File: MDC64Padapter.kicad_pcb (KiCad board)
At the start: 2 copper layers, 42.7 x 31 mm, 34 parts, among them J1 DB9_F_TO_C64, J2 DB9_M_TO_PAD, Q1 BC847, Q2 BC847, SW1 MODE, U1 74ACT08, U2 74ACT373, U3 74ACT157, U4 74ACT373, U5 74AHC1G04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

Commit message: Update PCB
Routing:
- net GND: track 242.2 -> 244.7 mm
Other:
- board text added: "Rev.0"
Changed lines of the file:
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@@
 		(tags "capacitor handsolder")
 		(property "Reference" "C7"
-			(at 0 0 0)
+			(at -2.54 -0.0885 90)
 			(layer "F.SilkS")
 			(effects
 				(font
-					(size 1 1)
-					(thickness 0.15)
+					(size 0.5 0.8)
+					(thickness 0.1)
 				)
 			)
 		)
 		(property "Value" "100nF"
-			(at 0 1.85 0)
-			(layer "F.Fab")
+			(at 0 0 0)
+			(layer "F.SilkS")
 			(effects
 				(font
-					(size 1 1)
-					(thickness 0.15)
+					(size 0.8 0.4)
+					(thickness 0.08)
 				)
 			)
@@
 		)
 		(property "Value" "10nF"
-			(at 0 1.85 90)
-			(layer "F.Fab")
+			(at 0 0 90)
+			(layer "F.SilkS")
 			(effects
 				(font
-					(size 1 1)
-					(thickness 0.15)
+					(size 0.8 0.5)
+					(thickness 0.1)
+					(bold yes)
 				)
 			)
@@
 		)
 		(property "Value" "10uF"
-			(at 0 1.85 90)
-			(layer "F.Fab")
+			(at 0 0 270)
+			(layer "F.SilkS")
 			(effects
 				(font
-					(size 1 1)
-					(thickness 0.15)
+					(size 0.8 0.5)
+					(thickness 0.08)
 				)
 			)
@@
 		(layer "Edge.Cuts")
 	)
+	(gr_text "Rev.0"
+		(at 65.151 128.397 0)
+		(layer "B.Cu")
+		(effects
+			(font
+				(size 1.5 1.5)
+				(thickness 0.3)
+				(bold yes)
+			)
+			(justify mirror)
+		)
+	)
 	(segment
 		(start 85.344 106.299)
@@
 	)
 	(segment
+		(start 69.53 129.86)
+		(end 68.792497 129.86)
+		(width 0.5)
+		(layer "B.Cu")
+		(net 2)
+	)
+	(segment
 		(start 61.341 124.841)
 		(end 61.341 114.935)
@@
 	)
 	(segment
+		(start 68.072 130.580497)
+		(end 68.072 130.81)
+		(width 0.5)
+		(layer "B.Cu")
+		(net 2)
+	)
+	(segment
 		(start 87.884 130.937)
 		(end 88.519 130.302)
@@
 	)
 	(segment
-		(start 66.929 126.099)
-		(end 66.929 129.286)
-		(width 0.5)
-		(layer "B.Cu")
-		(net 2)
-	)
-	(segment
 		(start 81.661 118.618)
 		(end 81.788 118.491)
@@
 	)
 	(segment
+		(start 68.072 130.81)
+		(end 65.659 130.81)
+		(width 0.5)
+		(layer "B.Cu")
+		(net 2)
+	)
+	(segment
+		(start 65.659 130.81)
+		(end 65.532 130.683)
+		(width 0.5)
+		(layer "B.Cu")
+		(net 2)
+	)
+	(segment
+		(start 69.7735 129.6165)
+		(end 69.53 129.86)
+		(width 0.5)
+		(layer "B.Cu")
+		(net 2)
+	)
+	(segment
 		(start 80.899 130.5)
 		(end 81.478 130.5)
@@
 	)
 	(segment
+		(start 69.7735 126.873)
+		(end 69.7735 129.6165)
+		(width 0.5)
+		(layer "B.Cu")
+		(net 2)
+	)
+	(segment
 		(start 59.17 114.947)
 		(end 60.059 114.058)
@@
 	)
 	(segment
+		(start 68.792497 129.86)
+		(end 68.072 130.580497)
+		(width 0.5)
+		(layer "B.Cu")
+		(net 2)
+	)
+	(segment
 		(start 76.454 107.696)
 		(end 76.454 115.189)
@@
 	)
 	(segment
-		(start 66.929 129.286)
-		(end 65.532 130.683)
-		(width 0.5)
-		(layer "B.Cu")
-		(net 2)
-	)
-	(segment
 		(start 64.77 102.108)
 		(end 66.802 102.108)
@@
 	)
 	(segment
+		(start 75.4985 120.4565)
+		(end 75.4985 120.0815)
+		(width 0.5)
+		(layer "F.Cu")
+		(net 4)
+	)
+	(segment
 		(start 62.865 123.444)
 		(end 59.855 123.444)
@@
 	)
 	(segment
+		(start 75.4985 120.0815)
+		(end 75.636 119.944)
+		(width 0.5)
+		(layer "F.Cu")
+		(net 4)
+	)
+	(segment
 		(start 80.518 110.2235)
 		(end 80.518 108.839)
@@
 	)
 	(segment
+		(start 88.265 118.237)
+		(end 91.44 118.237)
+		(width 0.5)
+		(layer "B.Cu")
+		(net 4)
+	)
+	(segment
+		(start 78.105 117.475)
+		(end 87.503 117.475)
+		(width 0.5)
+		(layer "B.Cu")
+		(net 4)
+	)
+	(segment
 		(start 78.8845 115.4605)
 		(end 79.397 115.4605)
@@
 	)
 	(segment
-		(start 86.614 107.823)
-		(end 83.439 107.823)
-		(width 0.5)
-		(layer "B.Cu")
-		(net 4)
-	)
-	(segment
-		(start 78.105 121.793)
-		(end 78.105 115.951)
+		(start 91.44 118.237)
+		(end 91.729 117.948)
 		(width 0.5)
 		(layer "B.Cu")
@@
 	)
 	(segment
-		(start 91.44 118.237)
-		(end 91.729 117.948)
+		(start 86.614 107.823)
+		(end 83.439 107.823)
 		(width 0.5)
 		(layer "B.Cu")
@@
 	)
 	(segment
-		(start 91.729 117.948)
-		(end 91.729 117.602)
+		(start 78.105 121.793)
+		(end 78.105 115.951)
 		(width 0.5)
 		(layer "B.Cu")
@@
 	)
 	(segment
-		(start 87.577 117.549)
-		(end 88.265 118.237)
-		(width 0.5)
-		(layer "B.Cu")
-		(net 4)
-	)
-	(segment
 		(start 91.313 110.744)
 		(end 91.059 110.49)
@@
 	)
 	(segment
-		(start 88.265 118.237)
-		(end 91.44 118.237)
-		(width 0.5)
-		(layer "B.Cu")
-		(net 4)
-	)
-	(segment
 		(start 85.763571 127.579214)
 		(end 91.876786 127.579214)
@@
 	)
 	(segment
-		(start 80.465 117.549)
-		(end 87.577 117.549)
+		(start 91.729 117.948)
+		(end 91.729 117.602)
 		(width 0.5)
 		(layer "B.Cu")
@@
 	)
 	(segment
-		(start 79.397 116.481)
-		(end 80.465 117.549)
+		(start 87.503 117.475)
+		(end 88.265 118.237)
 		(width 0.5)
 		(layer "B.Cu")
@@
 		(width 0.5)
 		(layer "B.Cu")
-		(net 4)
-	)
-	(segment
-		(start 79.397 115.4605)
-		(end 79.397 116.481)
-		(width 0.5)
-		(layer "B.Cu")

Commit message: Update PCB
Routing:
- net /MD_LEFT_M: track 21.8 -> 24.2 mm
- net /CLK: track 27.1 -> 26.4 mm
- net /MD_RIGHT_M: track 29.4 -> 28.7 mm

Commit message: Reorg
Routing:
- net GND: track 244.7 -> 248.5 mm, vias 29 -> 30
- net /MD_LEFT_M: track 24.2 -> 22.7 mm
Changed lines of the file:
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@@
 		)
 		(property "Value" "74ACT373"
-			(at 0.127 0 180)
+			(at 0 0 180)
 			(layer "F.SilkS")
 			(effects
@@
 	)
 	(segment
+		(start 68.58 104.394)
+		(end 68.58 107.442)
+		(width 0.3)
+		(layer "F.Cu")
+		(net 2)
+	)
+	(segment
 		(start 85.852 115.062)
 		(end 85.852 115.443)
@@
 	)
 	(via
+		(at 68.58 107.442)
+		(size 0.6)
+		(drill 0.3)
+		(layers "F.Cu" "B.Cu")
+		(net 2)
+	)
+	(via
 		(at 80.899 130.5)
 		(size 0.6)
@@
 	)
 	(segment
+		(start 60.059 114.058)
+		(end 60.059 113.665)
+		(width 0.5)
+		(layer "B.Cu")
+		(net 2)
+	)
+	(segment
 		(start 81.661 118.618)
 		(end 81.788 118.491)
@@
 	)
 	(segment
+		(start 60.579 114.173)
+		(end 60.071 113.665)
+		(width 0.5)
+		(layer "B.Cu")
+		(net 2)
+	)
+	(segment
 		(start 69.7735 129.6165)
 		(end 69.53 129.86)
@@
 	)
 	(segment
+		(start 60.579 114.173)
+		(end 60.452 114.046)
+		(width 0.5)
+		(layer "B.Cu")
+		(net 2)
+	)
+	(segment
 		(start 92.456 113.538)
 		(end 90.043 113.538)
@@
 	)
 	(segment
-		(start 61.341 114.935)
-		(end 60.452 114.046)
-		(width 0.5)
-		(layer "B.Cu")
-		(net 2)
-	)
-	(segment
 		(start 60.961409 102.760369)
 		(end 64.117631 102.760369)
@@
 	)
 	(segment
-		(start 88.646 112.014)
-		(end 86.36 112.014)
+		(start 61.341 114.935)
+		(end 60.579 114.173)
 		(width 0.5)
 		(layer "B.Cu")
@@
 	)
 	(segment
-		(start 60.059 114.058)
-		(end 60.059 103.662778)
+		(start 88.646 112.014)
+		(end 86.36 112.014)
 		(width 0.5)
 		(layer "B.Cu")
@@
 	)
 	(segment
+		(start 60.059 113.665)
+		(end 60.059 103.662778)
+		(width 0.5)
+		(layer "B.Cu")
+		(net 2)
+	)
+	(segment
 		(start 64.77 103.378)
 		(end 64.77 102.108)
@@
 	)
 	(segment
+		(start 60.071 113.665)
+		(end 60.059 113.665)
+		(width 0.5)
+		(layer "B.Cu")
+		(net 2)
+	)
+	(segment
 		(start 81.788 130.81)
 		(end 81.915 130.937)
@@
 	)
 	(segment
-		(start 92.205 114.049)
-		(end 92.329 114.173)
-		(width 0.2)
-		(layer "F.Cu")
-		(net 19)
-	)
-	(segment
 		(start 92.205 108.585)
 		(end 92.205 112.522)
@@
 	)
 	(segment
-		(start 89.027 123.571)
-		(end 89.027 127.127)
-		(width 0.2)
-		(layer "F.Cu")
-		(net 19)
-	)
-	(segment
 		(start 92.205 112.522)
 		(end 92.205 113.411)
@@
 	)
 	(segment
-		(start 86.604157 128.152843)
-		(end 86.604157 128.279843)
+		(start 92.205 114.049)
+		(end 92.329 114.173)
 		(width 0.2)
 		(layer "F.Cu")
@@
 	)
 	(segment
-		(start 86.604157 128.279843)
-		(end 86.207 128.677)
+		(start 88.519 127.635)
+		(end 87.122 127.635)
 		(width 0.2)
 		(layer "F.Cu")
@@
 	)
 	(segment
-		(start 87.122 127.635)
-		(end 86.604157 128.152843)
+		(start 92.329 118.823456)
+		(end 89.027 122.125456)
 		(width 0.2)
 		(layer "F.Cu")
@@
 	)
 	(segment
-		(start 92.356 113.562)
-		(end 92.205 113.411)
+		(start 89.027 127.127)
+		(end 88.519 127.635)
 		(width 0.2)
 		(layer "F.Cu")
@@
 	)
 	(segment
-		(start 92.329 118.823456)
-		(end 89.808 121.344456)
+		(start 86.604157 128.279843)
+		(end 86.207 128.677)
 		(width 0.2)
 		(layer "F.Cu")
@@
 	)
 	(segment
-		(start 89.027 127.127)
-		(end 88.519 127.635)
+		(start 92.356 113.562)
+		(end 92.205 113.411)
 		(width 0.2)
 		(layer "F.Cu")
@@
 	)
 	(segment
-		(start 92.329 114.173)
-		(end 92.329 118.823456)
+		(start 87.122 127.635)
+		(end 86.604157 128.152843)
 		(width 0.2)
 		(layer "F.Cu")
@@
 	)
 	(segment
-		(start 86.207 128.677)
-		(end 86.207 130.5)
+		(start 92.205 113.411)
+		(end 92.205 114.049)
 		(width 0.2)
 		(layer "F.Cu")
@@
 	)
 	(segment
-		(start 89.808 121.344456)
-		(end 89.808 122.79)
+		(start 86.207 128.677)
+		(end 86.207 130.5)
 		(width 0.2)
 		(layer "F.Cu")
@@
 	)
 	(segment
-		(start 92.205 113.411)
-		(end 92.205 114.049)
+		(start 86.604157 128.152843)
+		(end 86.604157 128.279843)
 		(width 0.2)
 		(layer "F.Cu")
@@
 	)
 	(segment
-		(start 89.808 122.79)
-		(end 89.027 123.571)
+		(start 89.027 122.125456)
+		(end 89.027 127.127)
 		(width 0.2)
 		(layer "F.Cu")
@@
 	)
 	(segment
-		(start 88.519 127.635)
-		(end 87.122 127.635)
+		(start 92.329 114.173)
+		(end 92.329 118.823456)
 		(width 0.2)
 		(layer "F.Cu")
@@
 	)
 	(segment
-		(start 86.013657 128.177657)
-		(end 86.013657 128.304657)
+		(start 91.220658 120.557658)
+		(end 91.093658 120.684658)
 		(width 0.2)
 		(layer "F.Cu")
@@
 	)
 	(segment
-		(start 91.020315 120.758)
-		(end 90.424 121.354315)
+		(start 86.956314 127.235)
+		(end 86.0121 128.179214)
 		(width 0.2)
 		(layer "F.Cu")
@@
 	)
 	(segment
-		(start 85.557 128.761314)
-		(end 85.557 130.5)
+		(start 91.020315 120.758)
+		(end 90.424 121.354315)
 		(width 0.2)
 		(layer "F.Cu")
@@
 	)
 	(segment
-		(start 88.392 126.981)
-		(end 88.138 127.235)
+		(start 86.0121 128.306214)
+		(end 85.557 128.761314)
 		(width 0.2)
 		(layer "F.Cu")
@@
 	)
 	(segment
-		(start 90.424 123.698)
-		(end 90.424 121.412)
+		(start 88.392 126.981)
+		(end 88.138 127.235)
 		(width 0.2)
 		(layer "F.Cu")
@@
 	)
 	(segment
-		(start 88.138 127.235)
-		(end 86.956314 127.235)
+		(start 85.557 128.761314)
+		(end 85.557 130.5)
 		(width 0.2)
 		(layer "F.Cu")
@@
 	)
 	(segment
-		(start 86.013657 128.304657)
-		(end 85.557 128.761314)
+		(start 91.093658 120.684658)
+		(end 91.020316 120.758)
 		(width 0.2)
 		(layer "F.Cu")
@@
 	)
 	(segment
-		(start 89.916 124.395)
-		(end 89.916 124.206)
+		(start 86.0121 128.179214)
+		(end 86.0121 128.306214)
 		(width 0.2)
 		(layer "F.Cu")
@@
 	)
 	(segment
-		(start 91.020316 120.758)
-		(end 91.020315 120.758)
+		(start 89.916 124.395)
+		(end 89.916 124.206)
 		(width 0.2)
 		(layer "F.Cu")
@@
 	)
 	(segment
-		(start 86.956314 127.235)
-		(end 86.013657 128.177657)
+		(start 91.020316 120.758)
+		(end 91.020315 120.758)
 		(width 0.2)
 		(layer "F.Cu")
@@
 	)
 	(segment
-		(start 92.808158 118.970158)
-		(end 92.808157 118.970158)
+		(start 88.138 127.235)
+		(end 86.956314 127.235)
 		(width 0.2)
 		(layer "F.Cu")
@@
 	)
 	(segment
-		(start 90.424 121.354315)
-		(end 90.424 123.444)
+		(start 90.051398 121.726918)
+		(end 91.093658 120.684658)
 		(width 0.2)
 		(layer "F.Cu")
@@
 	)
 	(segment
-		(start 88.392 124.495)
-		(end 88.392 126.981)
+		(start 92.808158 118.970158)
+		(end 92.808157 118.970158)
 		(width 0.2)
 		(layer "F.Cu")
@@
 	)
 	(segment
-		(start 92.808157 116.995843)
-		(end 93.472 116.332)
+		(start 88.427 124.46)
+		(end 88.392 124.495)
 		(width 0.2)
 		(layer "F.Cu")
@@
 	)
 	(segment
-		(start 91.220658 120.557658)
-		(end 91.020316 120.758)
+		(start 90.051398 123.921863)
+		(end 90.051398 121.726918)
 		(width 0.2)
 		(layer "F.Cu")
@@
 	)
 	(segment
-		(start 89.916 124.206)
-		(end 90.424 123.698)
+		(start 88.392 124.495)
+		(end 88.392 126.981)
 		(width 0.2)
 		(layer "F.Cu")
@@
 	)
 	(segment
-		(start 88.427 124.46)
-		(end 88.392 124.495)
+		(start 92.808157 116.995843)
+		(end 93.472 116.332)
 		(width 0.2)
 		(layer "F.Cu")

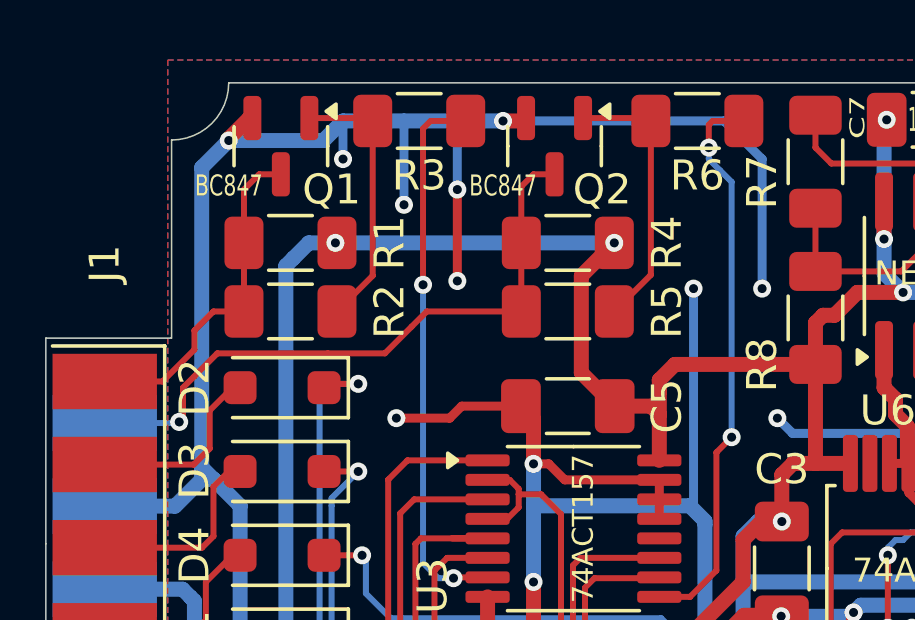
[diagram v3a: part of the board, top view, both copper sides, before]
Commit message: Add amiga compatibility
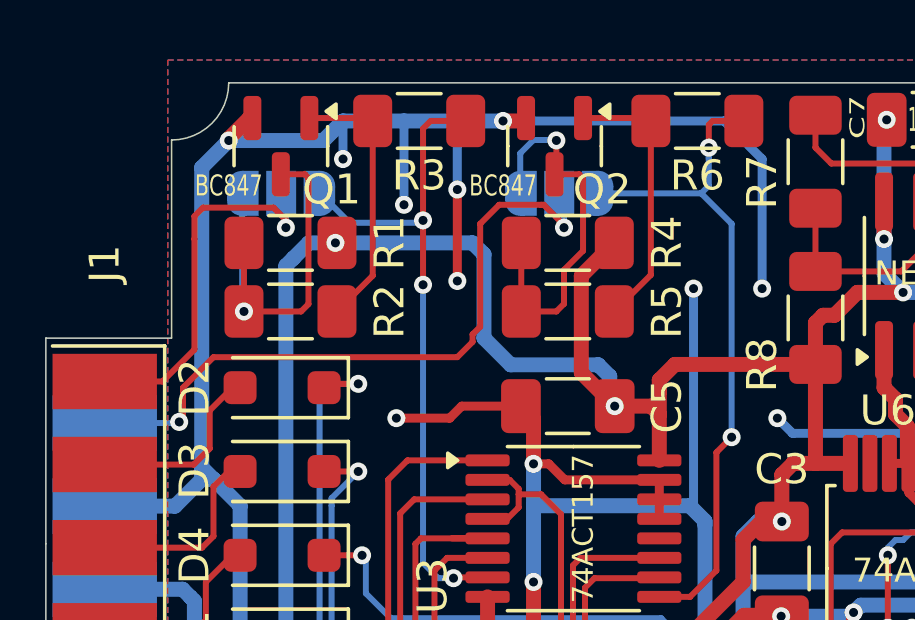
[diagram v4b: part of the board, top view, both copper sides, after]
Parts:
- added JP1: Amiga/C64 SEL1, Jumper:SolderJumper-3_P1.3mm_Open_RoundedPad1.0x1.5mm, B.Cu at (62.7, 104.5)
- added JP2: Amiga/C64 SEL2, Jumper:SolderJumper-3_P1.3mm_Open_RoundedPad1.0x1.5mm, B.Cu at (72.0, 104.5)
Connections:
- Q1 pad 3: /C64_POTY -> Net-(JP1-B)
- Q2 pad 3: /C64_POTX -> Net-(JP2-B)
- R1 pad 2: /C64_POTY -> Net-(JP1-B)
- R2 pad 2: /C64_POTY -> Net-(JP1-B)
- R4 pad 2: /C64_POTX -> Net-(JP2-B)
- R5 pad 2: /C64_POTX -> Net-(JP2-B)
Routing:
- net Net-(JP1-B): track 0.00 -> 13.7 mm, vias 0 -> 1
- net Net-(JP2-B): track 0.00 -> 13.2 mm, vias 0 -> 1
- net VCC: track 161.3 -> 165.7 mm
- net /C64_B: track 18.9 -> 22.9 mm
- net /C64_C: track 18.4 -> 22.2 mm, vias 2 -> 3
- net /C64_POTY: track 11.5 -> 12.7 mm, vias 0 -> 1
- net /C64_POTX: track 21.5 -> 22.6 mm, vias 1 -> 2
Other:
- board text added: "Pins 1-2: Amiga Pins 2-3: C64"
